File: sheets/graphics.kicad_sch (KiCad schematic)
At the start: 25 parts, among them J2 CUT DOG, SW1 RESET SWITCH, U13 NEO-B1, U14 PST518B, U15 74LS244, U16 TC531000AP, U17 uPD43256AGU-12L, U18 uPD43256AGU-12L, U19 CXK5864P-35, U20 CXK5864P-35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

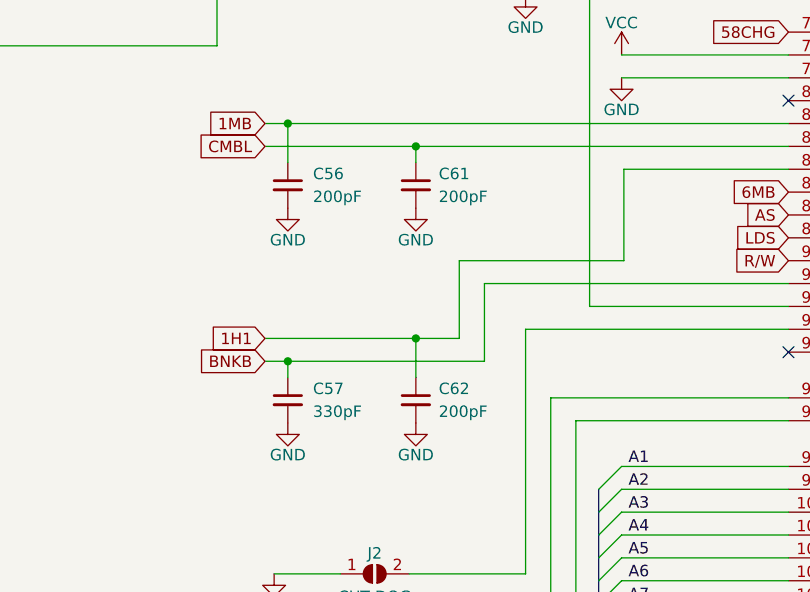
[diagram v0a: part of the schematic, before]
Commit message: Silkscreen layout updates
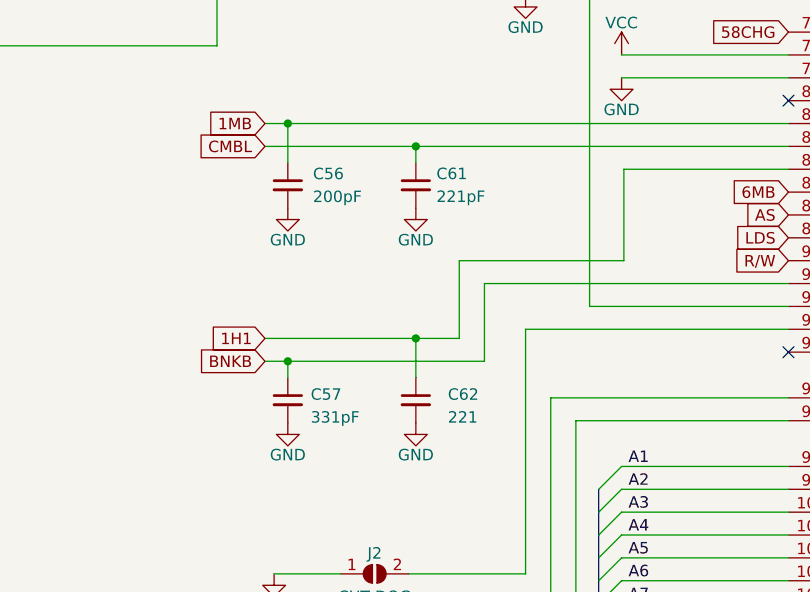
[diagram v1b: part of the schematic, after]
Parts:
- C57: value 330pF -> 331pF
- C61: value 200pF -> 221pF
- C62: value 200pF -> 221
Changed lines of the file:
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@@
   )
   (symbol (lib_id "Device:C_Small") (at 306.324 128.27 0) (unit 1)
-    (in_bom yes) (on_board yes) (dnp no) (fields_autoplaced)
-    (property "Reference" "C61" (at 308.864 127.0062 0)
-      (effects (font (size 1.27 1.27)) (justify left))
-    )
-    (property "Value" "200pF" (at 308.864 129.5462 0)
+    (in_bom yes) (on_board yes) (dnp no)
+    (property "Reference" "C61" (at 308.61 127 0)
+      (effects (font (size 1.27 1.27)) (justify left))
+    )
+    (property "Value" "221pF" (at 308.61 129.54 0)
       (effects (font (size 1.27 1.27)) (justify left))
     )
@@
   (symbol (lib_id "Device:C_Small") (at 306.324 152.146 0) (unit 1)
     (in_bom yes) (on_board yes) (dnp no) (fields_autoplaced)
-    (property "Reference" "C62" (at 308.864 150.8822 0)
-      (effects (font (size 1.27 1.27)) (justify left))
-    )
-    (property "Value" "200pF" (at 308.864 153.4222 0)
+    (property "Reference" "C62" (at 309.88 151.5173 0)
+      (effects (font (size 1.27 1.27)) (justify left))
+    )
+    (property "Value" "221" (at 309.88 154.0573 0)
       (effects (font (size 1.27 1.27)) (justify left))
     )
@@
   (symbol (lib_id "Device:C_Small") (at 292.1 152.146 0) (unit 1)
     (in_bom yes) (on_board yes) (dnp no) (fields_autoplaced)
-    (property "Reference" "C57" (at 294.894 150.8822 0)
-      (effects (font (size 1.27 1.27)) (justify left))
-    )
-    (property "Value" "330pF" (at 294.894 153.4222 0)
-      (effects (font (size 1.27 1.27)) (justify left))
-    )
+    (property "Reference" "C57" (at 294.64 151.5173 0)
+      (effects (font (size 1.27 1.27)) (justify left))
+    )
+    (property "Value" "331pF" (at 294.64 154.0573 0)
+      (effects (font (size 1.27 1.27)) (justify left))
+    )

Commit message: Final update to Schematics Footprints Silkscreens
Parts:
- C1: value 1uF -> 10uF
- C56: value 200pF -> 220pF
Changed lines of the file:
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@@
       (effects (font (size 1.27 1.27)) (justify left))
     )
-    (property "Value" "1uF" (at 320.294 105.664 0)
+    (property "Value" "10uF" (at 320.294 105.664 0)
       (effects (font (size 1.27 1.27)) (justify left))
     )
@@
   (symbol (lib_id "Device:C_Small") (at 292.1 128.27 0) (unit 1)
     (in_bom yes) (on_board yes) (dnp no) (fields_autoplaced)
-    (property "Reference" "C56" (at 294.894 127.0062 0)
-      (effects (font (size 1.27 1.27)) (justify left))
-    )
-    (property "Value" "200pF" (at 294.894 129.5462 0)
-      (effects (font (size 1.27 1.27)) (justify left))
-    )
+    (property "Reference" "C56" (at 294.64 127.6413 0)
+      (effects (font (size 1.27 1.27)) (justify left))
+    )
+    (property "Value" "220pF" (at 294.64 130.1813 0)
+      (effects (font (size 1.27 1.27)) (justify left))
+    )

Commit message: Some tweaks
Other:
- company: (none) -> SNK
- title: (none) -> NeoGeo AES
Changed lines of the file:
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@@
 (kicad_sch (version 20230121) (generator eeschema)
   (paper "A3")
+  (title_block
+    (title "NeoGeo AES")
+    (date "2023-08-19")
+    (rev "3.5")
+    (company "SNK")
+    (comment 3 "https://github.com/Board-Folk")
+    (comment 4 "Recreated By The Board Folk Team")
+  )
   (junction (at 301.752 185.166) (diameter 0) (color 0 0 0 0)
   )

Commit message: Updates to PCB Move P2 Joystick Port Move Memory Card Move Holes at top right Silkscreen added Update Titles
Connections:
- net EVEN: now also JP3.2 (B), U21.110 (EVN)
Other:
- title: NeoGeo AES -> NeoGeo AES 3-5
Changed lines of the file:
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@@
   (paper "A3")
   (title_block
-    (title "NeoGeo AES")
-    (date "2023-08-19")
-    (rev "3.5")
+    (title "NeoGeo AES 3-5")
+    (date "2023-08-27")
+    (rev "BF1.1")
     (company "SNK")
     (comment 3 "https://github.com/Board-Folk")
@@
   (junction (at 325.628 86.614) (diameter 0) (color 0 0 0 0)
   )
+  (junction (at 205.232 133.096) (diameter 0) (color 0 0 0 0)
+  )
   (junction (at 292.1 121.412) (diameter 0) (color 0 0 0 0)
   )
@@
   )
   (junction (at 373.126 187.452) (diameter 0) (color 0 0 0 0)
+  )
+  (junction (at 212.852 133.096) (diameter 0) (color 0 0 0 0)
   )
   (junction (at 31.242 252.476) (diameter 0) (color 0 0 0 0)
@@
     (stroke (width 0) (type default))
   )
+  (wire (pts (xy 212.852 133.096) (xy 212.852 130.302))
+    (stroke (width 0) (type default))
+  )
   (wire (pts (xy 212.09 84.836) (xy 204.724 84.836))
     (stroke (width 0) (type default))
@@
     (stroke (width 0) (type default))
   )
+  (wire (pts (xy 205.232 130.302) (xy 205.232 133.096))
+    (stroke (width 0) (type default))
+  )
   (bus (pts (xy 85.344 82.296) (xy 85.344 84.836))
     (stroke (width 0) (type default))
@@
     (stroke (width 0) (type default))
   )
+  (wire (pts (xy 212.852 130.302) (xy 205.232 130.302))
+    (stroke (width 0) (type default))
+  )

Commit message: Adding Mouser Part Numbers
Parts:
- C1: Mouser (none) -> 667-ECA-1CM100I
- C56, C61: Mouser (none) -> 810-FG28C0G1H221JNT0
- C57: Mouser (none) -> 810-FG28C0G1H331JNT6
- C58, C59: Mouser (none) -> 810-FG28C0G1H101JNT6
- C62: value 221 -> 221pF; Mouser (none) -> 810-FG28C0G1H221JNT0
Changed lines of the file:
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@@
+      (effects (font (size 1.27 1.27)) hide)
+    )
+    (property "Mouser" "" (at 60.198 77.216 0)
       (effects (font (size 1.27 1.27)) hide)
     )
@@
       (effects (font (size 1.27 1.27)))
     )
+    (property "Mouser" "" (at 222.25 77.216 0)
+      (effects (font (size 1.27 1.27)) hide)
+    )
     (pin "1")
     (pin "10")
@@
       (effects (font (size 1.27 1.27)) hide)
     )
+    (property "Mouser" "810-FG28C0G1H221JNT0" (at 306.324 128.27 0)
+      (effects (font (size 1.27 1.27)) hide)
+    )
     (pin "1")
     (pin "2")
@@
     )
     (property "Datasheet" "" (at 311.15 81.534 0)
+      (effects (font (size 1.27 1.27)) hide)
+    )
+    (property "Mouser" "" (at 311.15 86.614 0)
       (effects (font (size 1.27 1.27)) hide)
     )
@@
       (effects (font (size 1.27 1.27)) (justify left))
     )
-    (property "Value" "221" (at 309.88 154.0573 0)
+    (property "Value" "221pF" (at 309.88 154.0573 0)
       (effects (font (size 1.27 1.27)) (justify left))
     )
@@
       (effects (font (size 1.27 1.27)) hide)
     )
+    (property "Mouser" "810-FG28C0G1H221JNT0" (at 306.324 152.146 0)
+      (effects (font (size 1.27 1.27)) hide)
+    )
     (pin "1")
     (pin "2")
@@
       (effects (font (size 1.27 1.27)) hide)
     )
+    (property "Mouser" "" (at 301.498 57.912 0)
+      (effects (font (size 1.27 1.27)) hide)
+    )
     (pin "1")
     (pin "2")
@@
       (effects (font (size 1.27 1.27)) hide)
     )
+    (property "Mouser" "667-ECA-1CM100I" (at 318.516 104.648 0)
+      (effects (font (size 1.27 1.27)) hide)
+    )
     (pin "1")
     (pin "2")
@@
     )
     (property "Datasheet" "" (at 256.032 84.836 0)
+      (effects (font (size 1.27 1.27)) hide)
+    )
+    (property "Mouser" "" (at 256.032 84.836 0)
       (effects (font (size 1.27 1.27)) hide)
     )
@@
       (effects (font (size 1.27 1.27)) hide)
     )
+    (property "Mouser" "" (at 325.628 61.976 0)
+      (effects (font (size 1.27 1.27)) hide)
+    )
     (pin "1")
     (pin "2")
@@
     )
     (property "Datasheet" "" (at 45.212 242.316 0)
+      (effects (font (size 1.27 1.27)) hide)
+    )
+    (property "Mouser" "" (at 45.212 242.316 0)
       (effects (font (size 1.27 1.27)) hide)
     )
@@
       (effects (font (size 1.27 1.27)) hide)
     )
+    (property "Mouser" "" (at 209.042 133.096 0)
+      (effects (font (size 1.27 1.27)) hide)
+    )
     (pin "1")
     (pin "2")
@@
       (effects (font (size 1.27 1.27)) hide)
     )
+    (property "Mouser" "810-FG28C0G1H101JNT6" (at 301.752 192.024 0)
+      (effects (font (size 1.27 1.27)) hide)
+    )
     (pin "1")
     (pin "2")
@@
     (property "Datasheet" "" (at 352.806 54.102 0)
       (effects (font (size 1.27 1.27)) (justify left) hide)
+    )
+    (property "Mouser" "" (at 347.726 55.372 0)
+      (effects (font (size 1.27 1.27)) hide)
     )
     (pin "1")
@@
       (effects (font (size 1.27 1.27)) hide)
     )
+    (property "Mouser" "" (at 209.042 135.636 0)
+      (effects (font (size 1.27 1.27)) hide)
+    )
     (pin "1")
     (pin "2")
@@
     )
     (property "Datasheet" "" (at 301.752 171.45 0)
+      (effects (font (size 1.27 1.27)) hide)
+    )
+    (property "Mouser" "" (at 301.752 171.45 0)
       (effects (font (size 1.27 1.27)) hide)
     )
@@
       (effects (font (size 1.27 1.27)) hide)
     )
+    (property "Mouser" "810-FG28C0G1H331JNT6" (at 292.1 152.146 0)
+      (effects (font (size 1.27 1.27)) hide)
+    )
     (pin "1")
     (pin "2")
@@
       (effects (font (size 1.27 1.27)) hide)
     )
+    (property "Mouser" "810-FG28C0G1H221JNT0" (at 292.1 128.27 0)
+      (effects (font (size 1.27 1.27)) hide)
+    )
     (pin "1")
     (pin "2")
@@
     )
     (property "Datasheet" "" (at 45.212 188.976 0)
+      (effects (font (size 1.27 1.27)) hide)
+    )
+    (property "Mouser" "" (at 45.212 188.976 0)
       (effects (font (size 1.27 1.27)) hide)
     )
@@
     (property "Datasheet" "" (at 160.782 42.926 0)
       (effects (font (size 1.27 1.27)) (justify left) hide)
+    )
+    (property "Mouser" "" (at 155.702 44.196 0)
+      (effects (font (size 1.27 1.27)) hide)
     )
     (pin "1")
@@
       (effects (font (size 1.27 1.27)) hide)
     )
+    (property "Mouser" "" (at 86.614 221.488 0)
+      (effects (font (size 1.27 1.27)) hide)
+    )
     (pin "1")
     (pin "2")
@@
       (effects (font (size 1.27 1.27)) hide)
     )
+    (property "Mouser" "" (at 91.186 241.808 0)
+      (effects (font (size 1.27 1.27)) hide)
+    )
     (pin "1")
     (pin "2")
@@
     )
     (property "Datasheet" "" (at 86.614 208.534 0)
+      (effects (font (size 1.27 1.27)) hide)
+    )
+    (property "Mouser" "" (at 86.614 208.534 0)
       (effects (font (size 1.27 1.27)) hide)
     )
@@
       (effects (font (size 1.27 1.27)) hide)
     )
+    (property "Mouser" "810-FG28C0G1H101JNT6" (at 314.452 192.024 0)
+      (effects (font (size 1.27 1.27)) hide)
+    )
     (pin "1")
     (pin "2")
@@
     )
     (property "Datasheet" "" (at 60.198 133.096 0)
+      (effects (font (size 1.27 1.27)) hide)
+    )
+    (property "Mouser" "" (at 60.198 133.096 0)
       (effects (font (size 1.27 1.27)) hide)
     )
@@
       (effects (font (size 1.27 1.27)) hide)
     )
+    (property "Mouser" "" (at 318.516 97.282 0)
+      (effects (font (size 1.27 1.27)) hide)
+    )
